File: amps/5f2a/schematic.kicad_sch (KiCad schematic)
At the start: 31 parts, among them T2 SE 5k:8

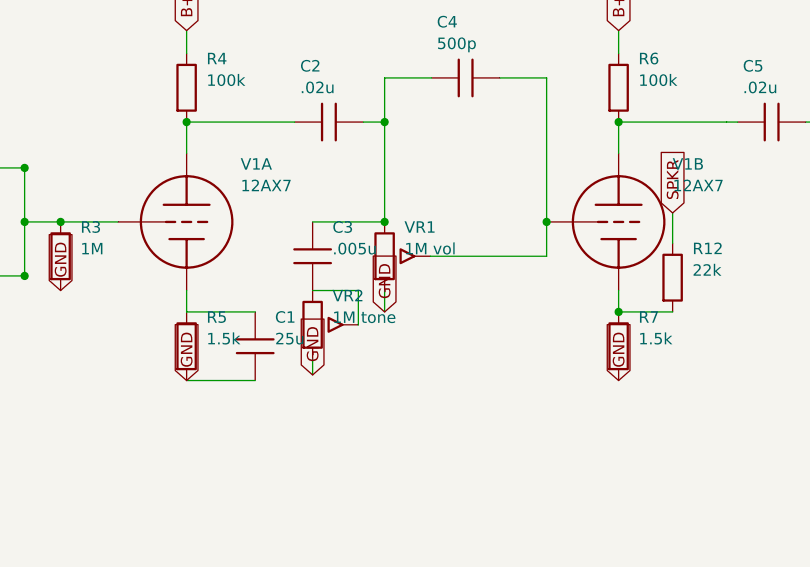
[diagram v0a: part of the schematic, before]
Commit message: Fix: schematic sheet polish — bias-supply and label crowding
- 5F4 + JTM45: lift bias-supply branch clear of the A4 title-block corner
- 5F2-A + 5F10: relieve tone-pot / cathodyne label crowding
- Regenerated schematics via draw_*.py; public/ mirrors synced by build

🤖 Generated with [Claude Code](https://claude.com/claude-code)

Co-Authored-By: Claude Opus 4.8 (1M context) <noreply@anthropic.com>
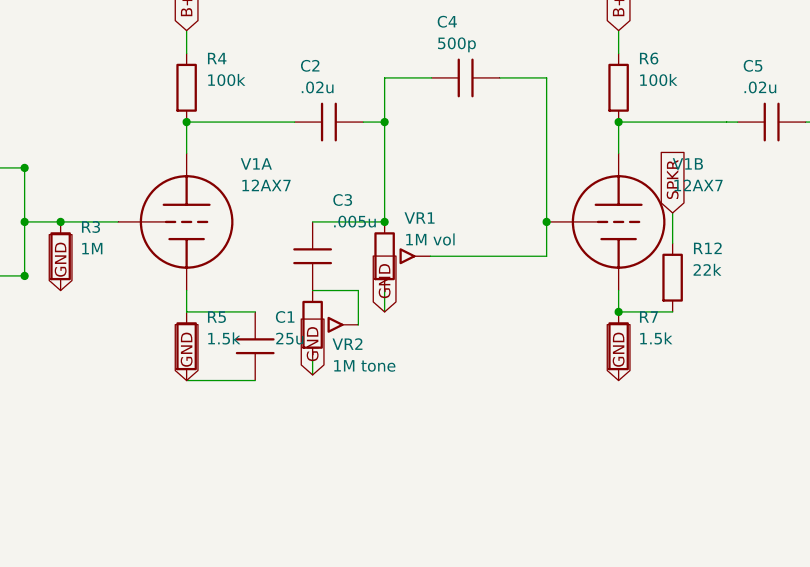
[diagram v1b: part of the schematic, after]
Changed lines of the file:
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@@
   (symbol (lib_id "cx:POT") (at 84 103.81 0) (unit 1)
     (in_bom yes) (on_board yes)
-    (property "Reference" "VR1" (at 86.2 100.61 0) (effects (font (size 1.27 1.27)) (justify left)))
-    (property "Value" "1M vol" (at 86.2 103.01 0) (effects (font (size 1.27 1.27)) (justify left))))
+    (property "Reference" "VR1" (at 86.2 99.61 0) (effects (font (size 1.27 1.27)) (justify left)))
+    (property "Value" "1M vol" (at 86.2 102.01 0) (effects (font (size 1.27 1.27)) (justify left))))
   (wire (pts (xy 84 107.62) (xy 84 110))
     (stroke (width 0) (type default)))
@@
   (symbol (lib_id "cx:C") (at 76 103.81 0) (unit 1)
     (in_bom yes) (on_board yes)
-    (property "Reference" "C3" (at 78.2 100.61 0) (effects (font (size 1.27 1.27)) (justify left)))
-    (property "Value" ".005u" (at 78.2 103.01 0) (effects (font (size 1.27 1.27)) (justify left))))
+    (property "Reference" "C3" (at 78.2 97.61 0) (effects (font (size 1.27 1.27)) (justify left)))
+    (property "Value" ".005u" (at 78.2 100.01 0) (effects (font (size 1.27 1.27)) (justify left))))
   (symbol (lib_id "cx:POT") (at 76 111.43 0) (unit 1)
     (in_bom yes) (on_board yes)
-    (property "Reference" "VR2" (at 78.2 108.23 0) (effects (font (size 1.27 1.27)) (justify left)))
-    (property "Value" "1M tone" (at 78.2 110.63 0) (effects (font (size 1.27 1.27)) (justify left))))
+    (property "Reference" "VR2" (at 78.2 113.63 0) (effects (font (size 1.27 1.27)) (justify left)))
+    (property "Value" "1M tone" (at 78.2 116.03 0) (effects (font (size 1.27 1.27)) (justify left))))
   (wire (pts (xy 81.08 111.43) (xy 81.08 107.62))
     (stroke (width 0) (type default)))

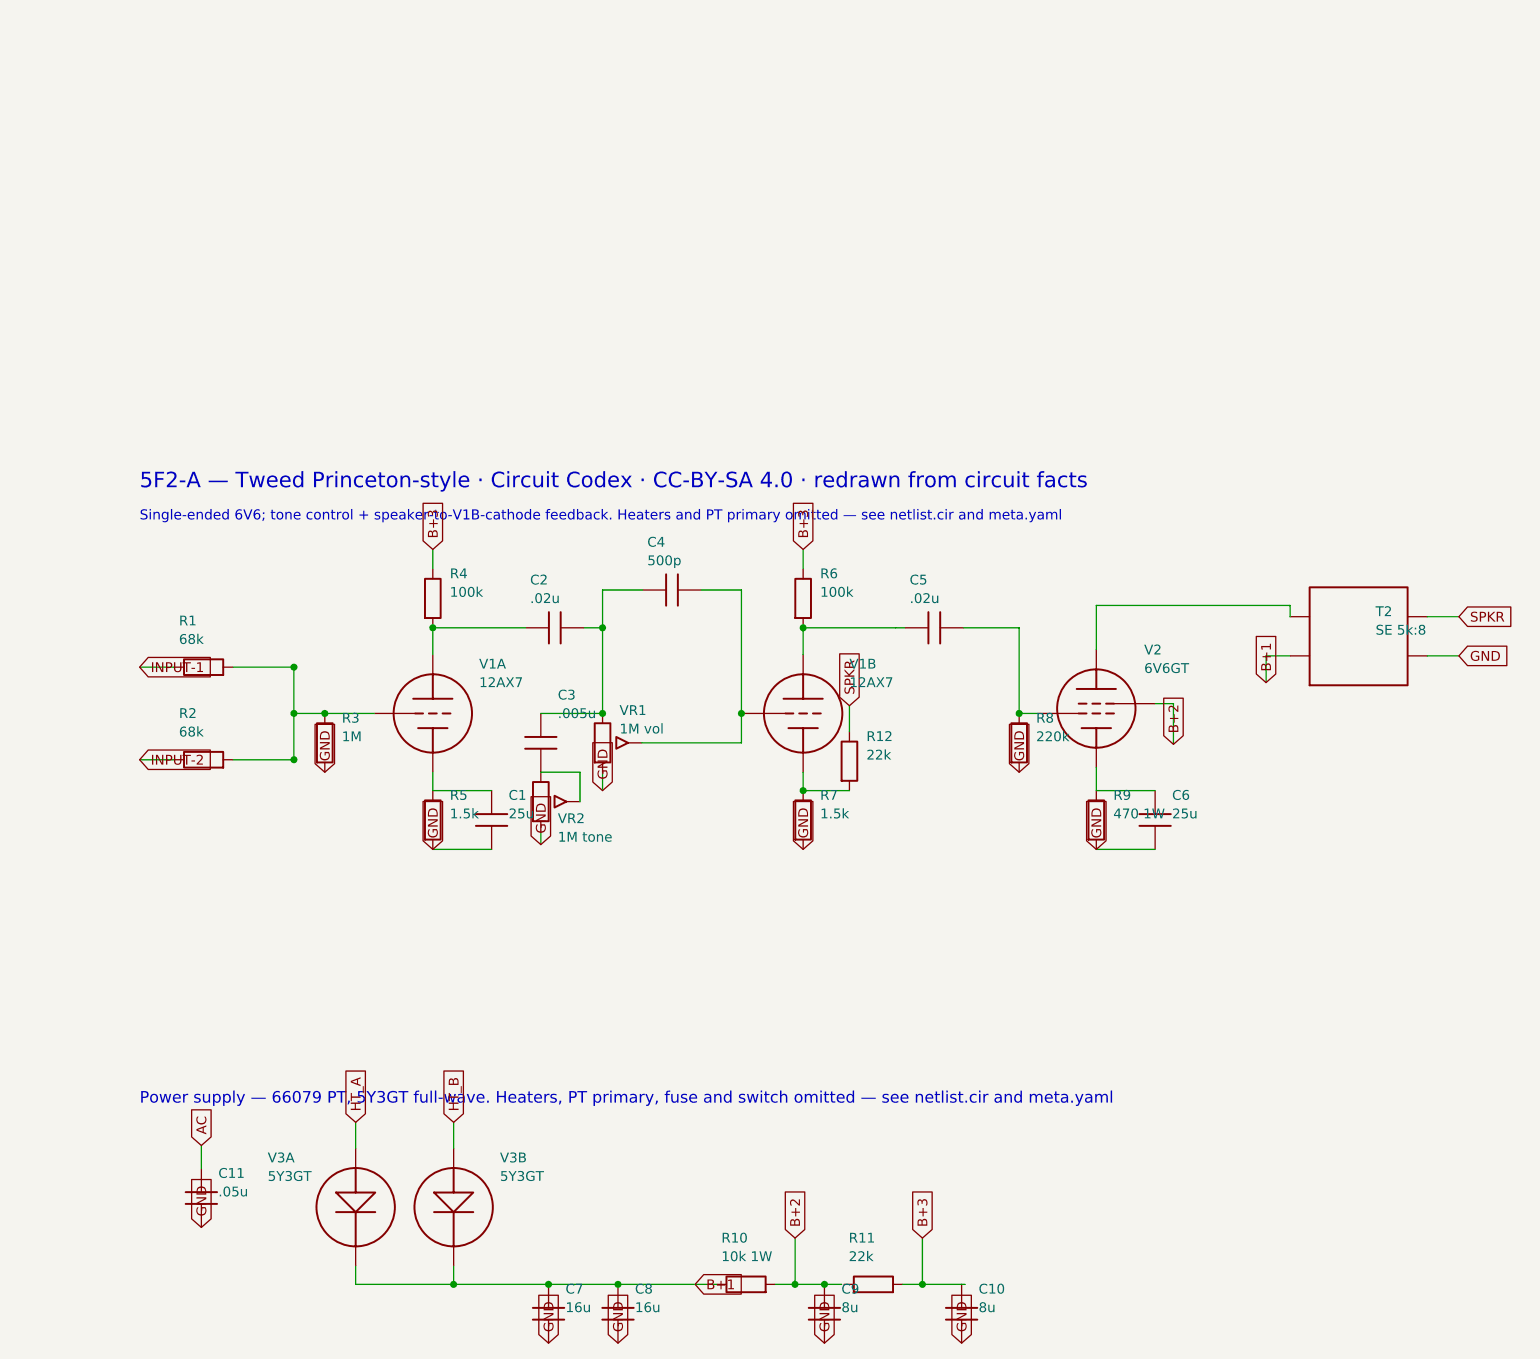
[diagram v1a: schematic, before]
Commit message: Fix: schematic sheets — real title block, fitted paper, no lettering through circuitry
Every sheet in the corpus shipped with an EMPTY title block ("Title:" and
"Date:" blank, default "Sheet /" furniture) laid onto a fixed A4/A3 page
regardless of the drawing's size, with prose annotations placed by hand
wherever a coordinate looked free when the amp was first drawn. The result
read as an unfinished alpha under a `verified` badge: KiCanvas's default view
is `zoom_to_page()`, so a 150 x 110 mm circuit on an A3 sheet opened as a
postage stamp, and later edits had pushed live circuitry under the prose.

schematic_lib.py — the builder now records each element as a (kind, points,
extra) tuple instead of a finished string, so `write()` can measure and move
what it emits:

- emits a real `(title_block …)` read from the amp's own meta.yaml — Title =
  designation + style, Date = the verification (or added) date, Rev = the
  verification status, Company = Circuit Codex, plus the licence and source
  URL as comments. Fixes all 34 sheets from one place;
- emits `(paper "User" w h)` cut to the drawing, translated to a fixed margin,
  with the bottom 34 mm strip reserved for the worksheet's title block. Sheet
  utilisation of the drawable area went from as low as ~20% to 92-98%;
- `note()` queues prose into a wrapped band under the circuit, and `caption()`
  places a section heading over the block it names, nudging it clear if it
  would print through anything;
- per-symbol default label offsets (the old single default printed every pot's
  value through its own wiper arrow and every transformer's designator through
  its body), plus `place_labels()`, which moves any designator/value block that
  would print over ink;
- transformers and chokes are drawn, not boxed: iron core between two windings,
  centre taps where the part has them, and an optional `spec` lettering slot for
  a ratio or impedance;
- `gnd()` takes a direction, because a flag defaulting to "down" at the HEAD of
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
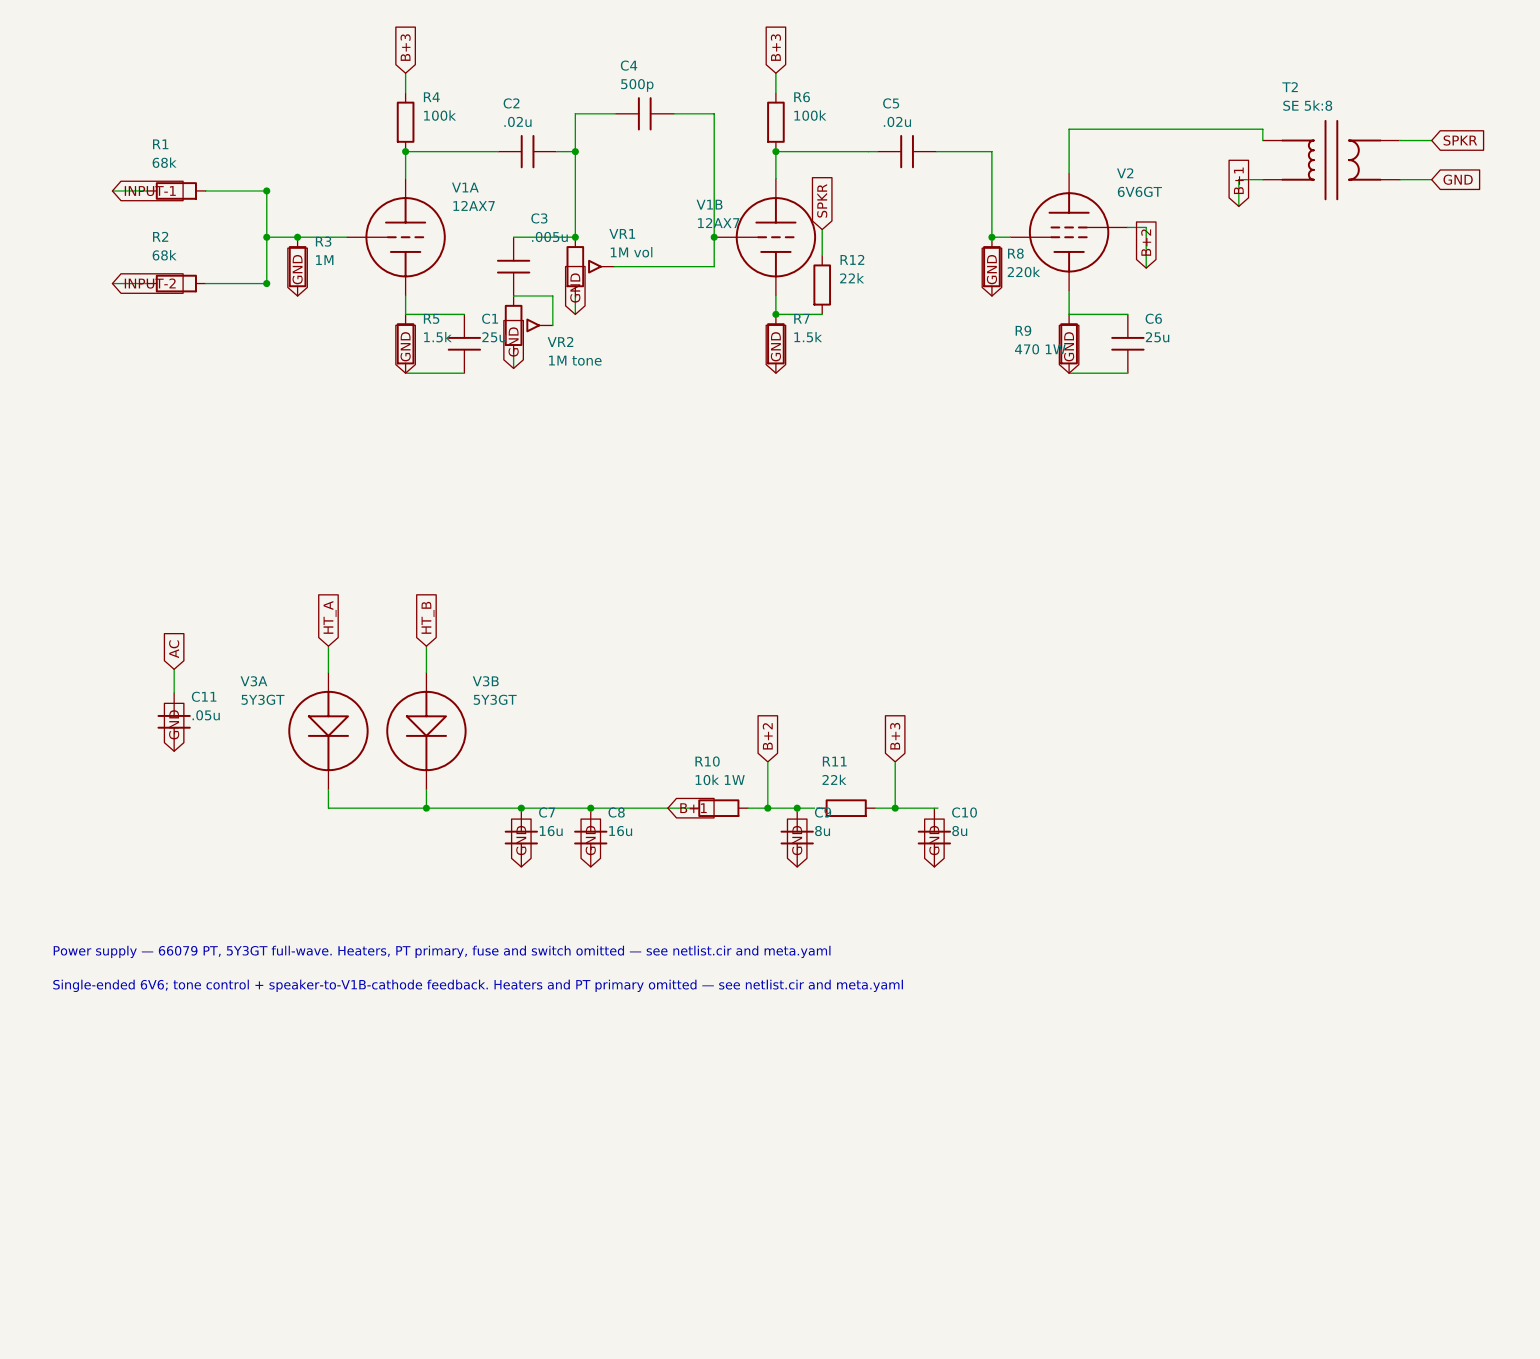
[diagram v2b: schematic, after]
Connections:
- net B+2: no longer R10.2
- net at C4.2, VR1.2 (W): no longer V1B.2 (G)
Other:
- note removed: "5F2-A — Tweed Princeton-style · Circuit Codex · CC-BY-SA 4.0 · redrawn from circuit facts"
- company: (none) -> Circuit Codex
- title: (none) -> 5F2-A — Tweed Princeton-style
